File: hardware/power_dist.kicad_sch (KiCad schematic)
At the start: 13 parts, among them U1 TPS62175DQC

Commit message: Fixed ERC errors & CAN module
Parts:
- C1: footprint (none) -> Capacitor_SMD:C_0603_1608Metric
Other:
- note added: "POWER DISTRIBUTION"
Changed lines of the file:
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@@
 	(generator_version "9.0")
 	(paper "A5")
+	(text "POWER DISTRIBUTION"
+		(exclude_from_sim no)
+		(at 109.728 21.336 0)
+		(effects
+			(font
+				(size 5.08 5.08)
+			)
+		)
+	)
 	(junction
 		(at 95.25 85.09)
@@
 			)
 			(justify right bottom)
-		)
-	)
-	(global_label "+5V"
-		(shape input)
-		(at 41.91 53.34 90)
-		(fields_autoplaced yes)
-		(effects
-			(font
-				(size 1.27 1.27)
-			)
-			(justify left)
-		)
-		(property "Intersheetrefs" "${INTERSHEET_REFS}"
-			(at 41.91 46.3892 90)
-			(effects
-				(font
-					(size 1.27 1.27)
-				)
-				(justify left)
-				(hide yes)
-			)
-		)
-	)
-	(global_label "+5V"
-		(shape input)
-		(at 166.37 45.72 90)
-		(fields_autoplaced yes)
-		(effects
-			(font
-				(size 1.27 1.27)
-			)
-			(justify left)
-		)
-		(property "Intersheetrefs" "${INTERSHEET_REFS}"
-			(at 166.37 38.7692 90)
-			(effects
-				(font
-					(size 1.27 1.27)
-				)
-				(justify left)
-				(hide yes)
-			)
 		)
 	)
@@
 			)
 			(justify right)
+		)
+	)
+	(symbol
+		(lib_id "power:+5V")
+		(at 41.91 53.34 0)
+		(unit 1)
+		(exclude_from_sim no)
+		(in_bom yes)
+		(on_board yes)
+		(dnp no)
+		(fields_autoplaced yes)
+		(property "Reference" "#PWR012"
+			(at 41.91 57.15 0)
+			(effects
+				(font
+					(size 1.27 1.27)
+				)
+				(hide yes)
+			)
+		)
+		(property "Value" "+5V"
+			(at 41.91 48.26 0)
+			(effects
+				(font
+					(size 1.27 1.27)
+				)
+			)
+		)
+		(property "Footprint" ""
+			(at 41.91 53.34 0)
+			(effects
+				(font
+					(size 1.27 1.27)
+				)
+				(hide yes)
+			)
+		)
+		(property "Datasheet" ""
+			(at 41.91 53.34 0)
+			(effects
+				(font
+					(size 1.27 1.27)
+				)
+				(hide yes)
+			)
+		)
+		(property "Description" "Power symbol creates a global label with name \"+5V\""
+			(at 41.91 53.34 0)
+			(effects
+				(font
+					(size 1.27 1.27)
+				)
+				(hide yes)
+			)
+		)
+		(pin "1"
+		)
+		(instances
+			(project "flight_stick"
+				(path "/594f9b09-cd7b-4dfb-a8eb-b099e26ad96c/bc2feb38-b1d3-42da-a90c-1ee53748a038"
+					(reference "#PWR012")
+					(unit 1)
+				)
+			)
 		)
 	)
@@
 			)
 		)
-		(property "Footprint" ""
+		(property "Footprint" "Capacitor_SMD:C_0603_1608Metric"
 			(at 68.2752 73.66 0)
 			(effects
@@
 					(unit 1)
 				)
+			)
+		)
+	)
+	(symbol
+		(lib_id "power:+5V")
+		(at 166.37 45.72 0)
+		(unit 1)
+		(exclude_from_sim no)
+		(in_bom yes)
+		(on_board yes)
+		(dnp no)
+		(fields_autoplaced yes)
+		(property "Reference" "#PWR09"
+			(at 166.37 49.53 0)
+			(effects
+				(font
+					(size 1.27 1.27)
+				)
+				(hide yes)
+			)
+		)
+		(property "Value" "+5V"
+			(at 166.37 40.64 0)
+			(effects
+				(font
+					(size 1.27 1.27)
+				)
+			)
+		)
+		(property "Footprint" ""
+			(at 166.37 45.72 0)
+			(effects
+				(font
+					(size 1.27 1.27)
+				)
+				(hide yes)
+			)
+		)
+		(property "Datasheet" ""
+			(at 166.37 45.72 0)
+			(effects
+				(font
+					(size 1.27 1.27)
+				)
+				(hide yes)
+			)
+		)
+		(property "Description" "Power symbol creates a global label with name \"+5V\""
+			(at 166.37 45.72 0)
+			(effects
+				(font
+					(size 1.27 1.27)
+				)
+				(hide yes)
+			)
+		)
+		(pin "1"
+		)
+		(instances
+			(project ""
+				(path "/594f9b09-cd7b-4dfb-a8eb-b099e26ad96c/bc2feb38-b1d3-42da-a90c-1ee53748a038"
+					(reference "#PWR09")
+					(unit 1)
+				)

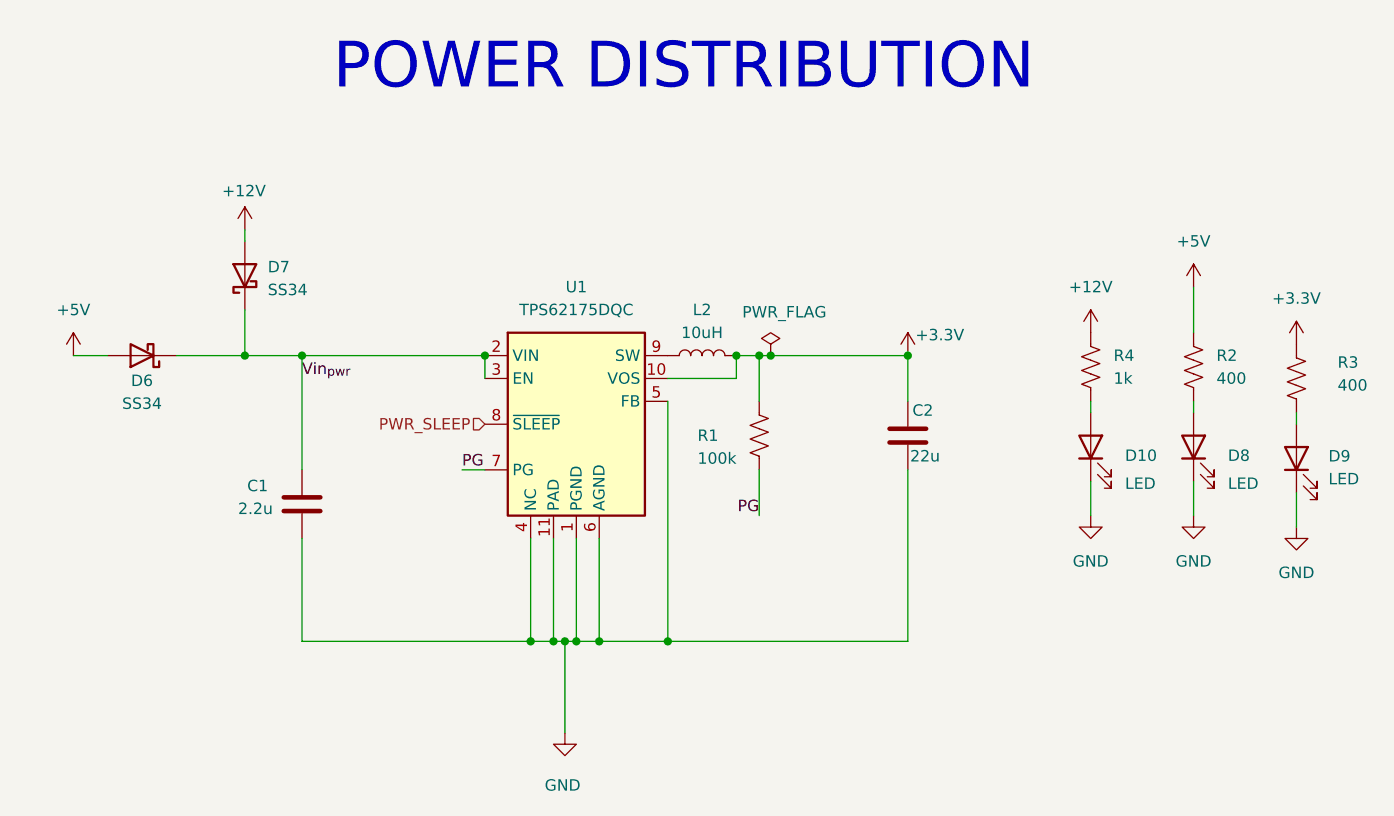
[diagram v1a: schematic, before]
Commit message: Added EEPROM, resolved comments
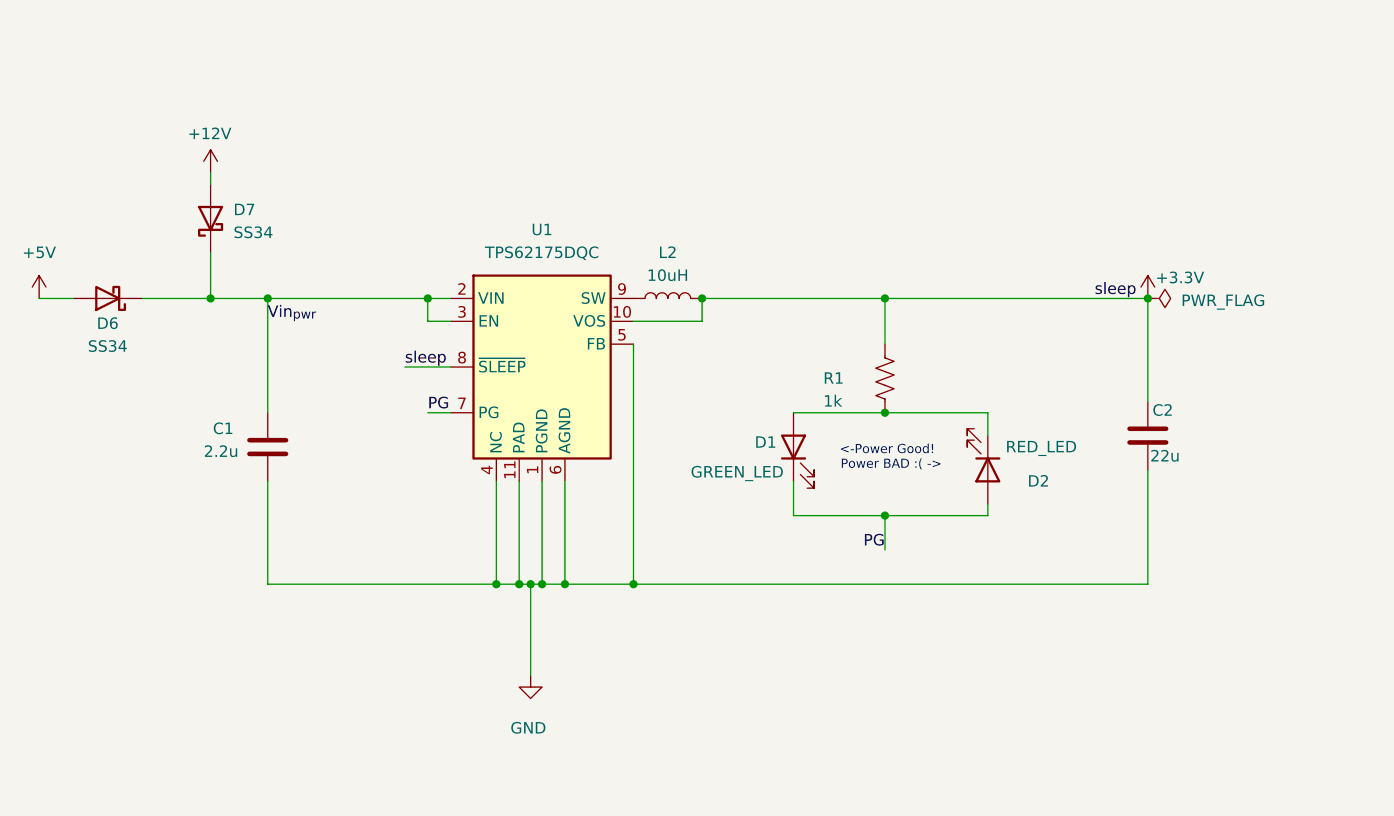
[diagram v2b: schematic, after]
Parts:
- removed D10, D8, D9: LED, LED_SMD:LED_0805_2012Metric, symbol Device:LED
- removed R2, R3: 400, Resistor_SMD:R_0603_1608Metric, symbol Device:R_US
- removed R4: 1k, Resistor_SMD:R_0603_1608Metric, symbol Device:R_US
- added D1: GREEN_LED, LED_SMD:LED_0805_2012Metric, symbol Device:LED
- added D2: RED_LED, LED_SMD:LED_0805_2012Metric, symbol Device:LED
- R1: value 100k -> 1k
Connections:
- net PWR_SLEEP is gone; now on net +3.3V: U1.8 (~{SLEEP})
- net PG: now also D1.1 (K), D2.2 (A); no longer R1.2
- new net: D1.2 (A), D2.1 (K), R1.2
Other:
- note added: "<-Power Good! Power BAD :( ->"
- note removed: "POWER DISTRIBUTION"
- company: (none) -> University of Toronto Human Powered Vehicles
- title: (none) -> Power distribution subsystem
- moved on the sheet: C1, C2, D6, D7, L2, R1, U1

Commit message: revamped button matrix
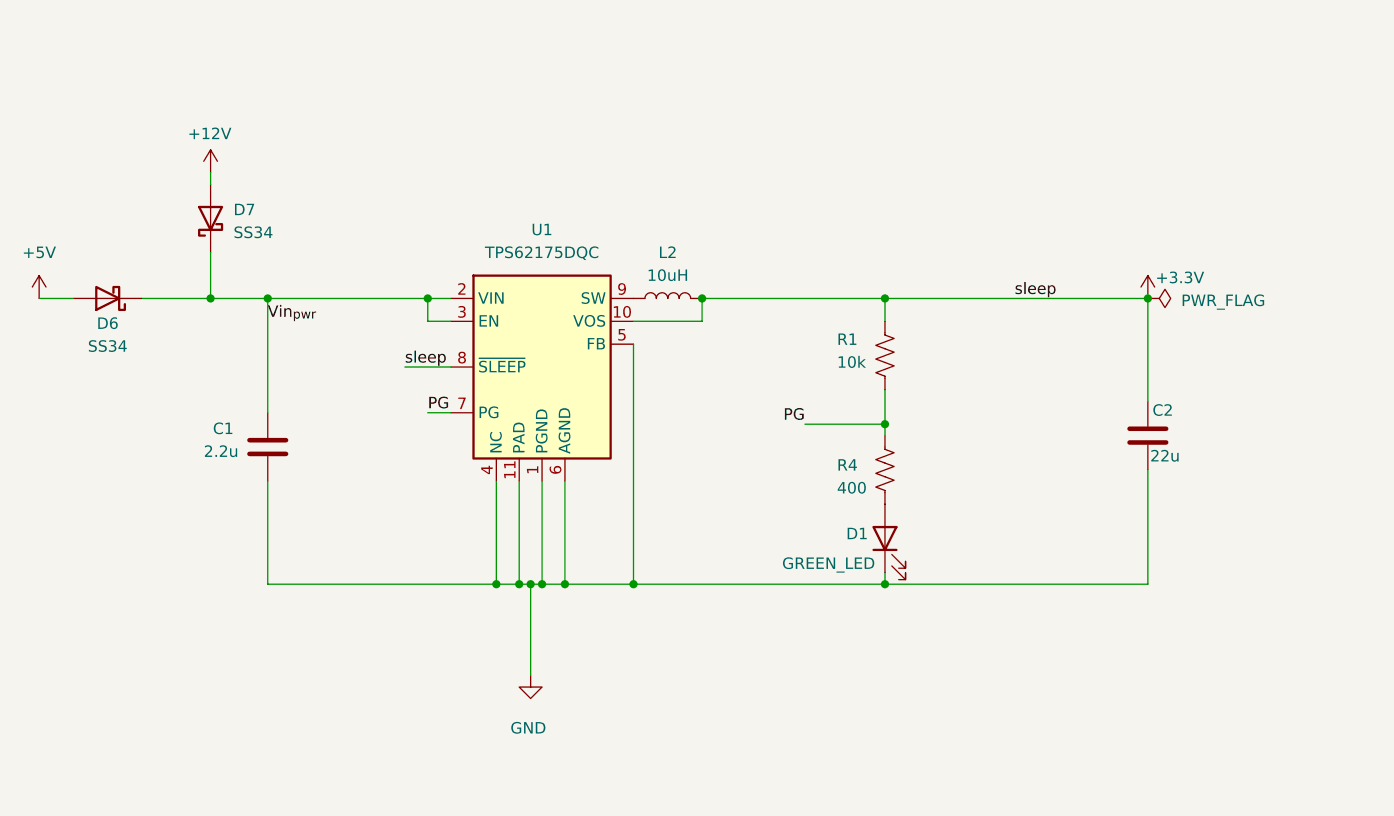
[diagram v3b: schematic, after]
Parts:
- removed D2: RED_LED, LED_SMD:LED_0805_2012Metric, symbol Device:LED
- added R4: 400, Resistor_SMD:R_0603_1608Metric, symbol Device:R_US
- R1: value 1k -> 10k
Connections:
- net GND: now also D1.1 (K)
- net PG: now also R1.2, R4.1; no longer D1.1 (K)
- net at D1.2 (A): now also R4.2; no longer R1.2
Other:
- note removed: "<-Power Good! Power BAD :( ->"
- moved on the sheet: D1, R1
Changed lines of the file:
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@@
 		(company "University of Toronto Human Powered Vehicles")
-	)
-	(text "<-Power Good!\n  Power BAD :( ->"
-		(exclude_from_sim no)
-		(at 132.334 64.77 0)
-		(effects
-			(font
-				(size 1.016 1.016)
-			)
-		)
 	)
 	(junction
@@
 	)
 	(junction
-		(at 132.08 59.69)
-		(diameter 0)
-		(color 0 0 0 0)
-	)
-	(junction
 		(at 93.98 78.74)
 		(diameter 0)
@@
 	)
 	(junction
-		(at 132.08 71.12)
+		(at 132.08 78.74)
 		(diameter 0)
 		(color 0 0 0 0)
@@
 	)
 	(junction
+		(at 132.08 60.96)
+		(diameter 0)
+		(color 0 0 0 0)
+	)
+	(junction
 		(at 111.76 46.99)
 		(diameter 0)
@@
 	(wire
 		(pts
-			(xy 132.08 71.12) (xy 121.92 71.12)
-		)
-		(stroke
-			(width 0)
-			(type default)
-		)
-	)
-	(wire
-		(pts
 			(xy 88.9 78.74) (xy 91.44 78.74)
 		)
@@
 	(wire
 		(pts
-			(xy 161.29 46.99) (xy 132.08 46.99)
+			(xy 123.19 60.96) (xy 132.08 60.96)
 		)
 		(stroke
@@
 	(wire
 		(pts
-			(xy 121.92 59.69) (xy 132.08 59.69)
-		)
-		(stroke
-			(width 0)
-			(type default)
-		)
-	)
-	(wire
-		(pts
 			(xy 93.98 78.74) (xy 96.52 78.74)
 		)
@@
 	(wire
 		(pts
+			(xy 132.08 60.96) (xy 132.08 62.23)
+		)
+		(stroke
+			(width 0)
+			(type default)
+		)
+	)
+	(wire
+		(pts
 			(xy 57.15 34.29) (xy 57.15 33.02)
 		)
@@
 	(wire
 		(pts
-			(xy 143.51 62.23) (xy 143.51 59.69)
-		)
-		(stroke
-			(width 0)
-			(type default)
-		)
-	)
-	(wire
-		(pts
 			(xy 81.28 46.99) (xy 81.28 49.53)
 		)
@@
 	(wire
 		(pts
-			(xy 132.08 71.12) (xy 143.51 71.12)
-		)
-		(stroke
-			(width 0)
-			(type default)
-		)
-	)
-	(wire
-		(pts
-			(xy 143.51 69.85) (xy 143.51 71.12)
-		)
-		(stroke
-			(width 0)
-			(type default)
-		)
-	)
-	(wire
-		(pts
-			(xy 104.14 78.74) (xy 161.29 78.74)
+			(xy 132.08 60.96) (xy 132.08 57.15)
+		)
+		(stroke
+			(width 0)
+			(type default)
+		)
+	)
+	(wire
+		(pts
+			(xy 104.14 78.74) (xy 132.08 78.74)
 		)
 		(stroke
@@
 	(wire
 		(pts
-			(xy 143.51 59.69) (xy 132.08 59.69)
-		)
-		(stroke
-			(width 0)
-			(type default)
-		)
-	)
-	(wire
-		(pts
 			(xy 96.52 67.31) (xy 96.52 78.74)
 		)
@@
 	(wire
 		(pts
-			(xy 132.08 71.12) (xy 132.08 74.93)
+			(xy 132.08 78.74) (xy 161.29 78.74)
+		)
+		(stroke
+			(width 0)
+			(type default)
+		)
+	)
+	(wire
+		(pts
+			(xy 132.08 77.47) (xy 132.08 78.74)
 		)
 		(stroke
@@
 	(wire
 		(pts
+			(xy 132.08 46.99) (xy 161.29 46.99)
+		)
+		(stroke
+			(width 0)
+			(type default)
+		)
+	)
+	(wire
+		(pts
 			(xy 63.5 67.31) (xy 63.5 78.74)
 		)
@@
 	(wire
 		(pts
-			(xy 121.92 71.12) (xy 121.92 67.31)
-		)
-		(stroke
-			(width 0)
-			(type default)
-		)
-	)
-	(wire
-		(pts
 			(xy 57.15 46.99) (xy 63.5 46.99)
 		)
@@
 	(wire
 		(pts
-			(xy 132.08 52.07) (xy 132.08 46.99)
+			(xy 132.08 49.53) (xy 132.08 46.99)
 		)
 		(stroke
@@
 	)
 	(label "sleep"
-		(at 160.02 46.99 180)
+		(at 151.13 46.99 180)
 		(effects
 			(font
@@
 	)
 	(label "PG"
-		(at 132.08 74.93 180)
+		(at 123.19 60.96 180)
 		(effects
 			(font
@@
 	)
 	(symbol
+		(lib_id "Device:R_US")
+		(at 132.08 66.04 0)
+		(unit 1)
+		(exclude_from_sim no)
+		(in_bom yes)
+		(on_board yes)
+		(dnp no)
+		(property "Reference" "R4"
+			(at 126.746 65.532 0)
+			(effects
+				(font
+					(size 1.27 1.27)
+				)
+				(justify left)
+			)
+		)
+		(property "Value" "400"
+			(at 126.746 68.072 0)
+			(effects
+				(font
+					(size 1.27 1.27)
+				)
+				(justify left)
+			)
+		)
+		(property "Footprint" "Resistor_SMD:R_0603_1608Metric"
+			(at 133.096 66.294 90)
+			(effects
+				(font
+					(size 1.27 1.27)
+				)
+				(hide yes)
+			)
+		)
+		(property "Datasheet" "~"
+			(at 132.08 66.04 0)
+			(effects
+				(font
+					(size 1.27 1.27)
+				)
+				(hide yes)
+			)
+		)
+		(property "Description" "Resistor, US symbol"
+			(at 132.08 66.04 0)
+			(effects
+				(font
+					(size 1.27 1.27)
+				)
+				(hide yes)
+			)
+		)
+		(property "LCSC" "C8218"
+			(at 132.08 66.04 0)
+			(effects
+				(font
+					(size 1.27 1.27)
+				)
+				(hide yes)
+			)
+		)
+		(pin "1"
+		)
+		(pin "2"
+		)
+		(instances
+			(project "flight_stick"
+				(path "/594f9b09-cd7b-4dfb-a8eb-b099e26ad96c/bc2feb38-b1d3-42da-a90c-1ee53748a038"
+					(reference "R4")
+					(unit 1)
+				)
+			)
+		)
+	)
+	(symbol
 		(lib_id "Device:L")
 		(at 107.95 46.99 90)
@@
 	(symbol
 		(lib_id "Device:LED")
-		(at 121.92 63.5 90)
+		(at 132.08 73.66 90)
 		(unit 1)
 		(exclude_from_sim no)
@@
 		(dnp no)
 		(property "Reference" "D1"
-			(at 117.602 62.992 90)
+			(at 127.762 73.152 90)
 			(effects
 				(font
@@
 		)
 		(property "Value" "GREEN_LED"
-			(at 110.49 66.294 90)
+			(at 120.65 76.454 90)
 			(effects
 				(font
@@
 		)
 		(property "Footprint" "LED_SMD:LED_0805_2012Metric"
-			(at 121.92 63.5 0)
+			(at 132.08 73.66 0)
 			(effects
 				(font
@@
 		)
 		(property "Datasheet" "~"
-			(at 121.92 63.5 0)
+			(at 132.08 73.66 0)
 			(effects
 				(font
@@
 		)
 		(property "Description" "Light emitting diode"
-			(at 121.92 63.5 0)
+			(at 132.08 73.66 0)
 			(effects
 				(font
@@
 		)
 		(property "LCSC" "C965818"
-			(at 121.92 63.5 0)
+			(at 132.08 73.66 0)
 			(effects
 				(font
@@
 	(symbol
 		(lib_id "Device:R_US")
-		(at 132.08 55.88 0)
+		(at 132.08 53.34 0)
 		(unit 1)
 		(exclude_from_sim no)
@@
 		(dnp no)
 		(property "Reference" "R1"
-			(at 125.222 55.88 0)
+			(at 126.746 51.562 0)
 			(effects
 				(font
@@
 			)
 		)
-		(property "Value" "1k"
-			(at 125.222 58.42 0)
+		(property "Value" "10k"
+			(at 126.746 54.102 0)
 			(effects
 				(font
@@
 		)
 		(property "Footprint" "Resistor_SMD:R_0603_1608Metric"
-			(at 133.096 56.134 90)
+			(at 133.096 53.594 90)
 			(effects
 				(font
@@
 		)
 		(property "Datasheet" "~"
-			(at 132.08 55.88 0)
+			(at 132.08 53.34 0)
 			(effects
 				(font
@@
 		)
 		(property "Description" "Resistor, US symbol"
-			(at 132.08 55.88 0)
+			(at 132.08 53.34 0)
 			(effects
 				(font
@@
 		)
 		(property "LCSC" "C8218"
-			(at 132.08 55.88 0)
+			(at 132.08 53.34 0)
 			(effects
 				(font
@@
 					(unit 1)
 				)
-			)
-		)
-	)
-	(symbol
-		(lib_id "Device:LED")
-		(at 143.51 66.04 270)
-		(unit 1)
-		(exclude_from_sim no)
-		(in_bom yes)
-		(on_board yes)
-		(dnp no)
-		(property "Reference" "D2"
-			(at 150.368 67.31 90)
-			(effects
-				(font
-					(size 1.27 1.27)
-				)
-				(justify right)
-			)
-		)
-		(property "Value" "RED_LED"
-			(at 153.416 63.5 90)
-			(effects
-				(font
-					(size 1.27 1.27)
-				)
-				(justify right)
-			)
-		)
-		(property "Footprint" "LED_SMD:LED_0805_2012Metric"
-			(at 143.51 66.04 0)
-			(effects
-				(font
-					(size 1.27 1.27)
-				)
-				(hide yes)
-			)
-		)
-		(property "Datasheet" "~"
-			(at 143.51 66.04 0)
-			(effects
-				(font
-					(size 1.27 1.27)
-				)
-				(hide yes)
-			)
-		)
-		(property "Description" "Light emitting diode"
-			(at 143.51 66.04 0)
-			(effects
-				(font
-					(size 1.27 1.27)
-				)
-				(hide yes)
-			)
-		)
-		(property "LCSC" "C965818"
-			(at 143.51 66.04 0)
-			(effects
-				(font
-					(size 1.27 1.27)
-				)
-				(hide yes)
-			)
-		)
-		(pin "1"
-		)
-		(pin "2"
-		)
-		(instances
-			(project "flight_stick"
-				(path "/594f9b09-cd7b-4dfb-a8eb-b099e26ad96c/bc2feb38-b1d3-42da-a90c-1ee53748a038"
-					(reference "D2")
-					(unit 1)
-				)

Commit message: Finished footprint assignment and deleted pcb
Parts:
- L2: footprint (none) -> Inductor_SMD:L_0603_1608Metric; LCSC (none) -> C86083
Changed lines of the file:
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@@
 			)
 		)
-		(property "Footprint" ""
+		(property "Footprint" "Inductor_SMD:L_0603_1608Metric"
 			(at 107.95 46.99 0)
 			(effects
@@
 			(effects
 				(font
+					(size 1.27 1.27)
+				)
+				(hide yes)
+			)
+		)
+		(property "LCSC" "C86083"
+			(at 107.95 46.99 90)
+			(effects
+				(font

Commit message: Completed first layout draft
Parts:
- added C3: 2.2u, Capacitor_SMD:C_0603_1608Metric, symbol Device:C
- R1: value 10k -> 100k
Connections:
- net +3.3V: now also R4.1
- net GND: now also C3.2
- net PG: no longer R4.1
- net Vin_{pwr}: now also C3.1
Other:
- moved on the sheet: D1, R1, R4

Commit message: resolved comments
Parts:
- added C4: 10n, Capacitor_SMD:C_0603_1608Metric, symbol Device:C
- added C5: 1u, Capacitor_SMD:C_0603_1608Metric, symbol Device:C
- added NT1: NetTie_2, NetTie:NetTie-2_THT_Pad1.0mm, symbol Device:NetTie_2
- added U7: LT1962-3.3, Package_SO:MSOP-8_3x3mm_P0.65mm, symbol Regulator_Linear:LT1962-3.3
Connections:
- net GND: now also NT1.2
- net Vin_{pwr}: now also C5.1, U7.8 (IN)
- new net: C4.2, U7.3 (BYP)
- new net +3.3VA: C4.1, U7.1 (OUT), U7.2 (SENSE)
- new net GNDA: C5.2, NT1.1, U7.4 (GND), U7.5 (~{SHDN})
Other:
- moved on the sheet: C1, C2, C3, D1, D6, D7, L2, R1, R4, U1

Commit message: Resolved comments
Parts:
- added C6: 4.7u, Capacitor_SMD:C_0603_1608Metric, symbol Device:C
- C1, C3: LCSC (none) -> C23630
- C2: LCSC C90806 -> C2762594
- C4: LCSC (none) -> C1589
- C5: LCSC (none) -> C15849
- D1: LCSC C965818 -> C84260
- D6, D7: footprint Diode_SMD:D_SMA -> Diode_SMD:D_SMC; LCSC (none) -> C154551
- R1: LCSC C8218 -> C14675
- R4: footprint Resistor_SMD:R_0603_1608Metric -> Resistor_SMD:R_0805_2012Metric; LCSC C8218 -> C153298
- U1: LCSC (none) -> C32097
- U7: LCSC (none) -> C665666
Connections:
- net +3.3VA: now also C6.1
- net GNDA: now also C6.2
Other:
- moved on the sheet: C1, C2, C3, C4, C5, D1, D6, D7, L2, NT1, R1, R4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
